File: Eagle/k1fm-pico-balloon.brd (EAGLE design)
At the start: 26.4 x 41.1 mm, 42 parts, among them J1 I2C, J2 ICSP, J3 SERIAL, J4 POWER, Q1 ASTX-H11-25.000MHZ-T, Q2 DMP2305U, Q3 DMP2305U, U1 ATMEGA328, U2 Si5351A-B-GT, U3 MCP1754X-XXXXX/C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

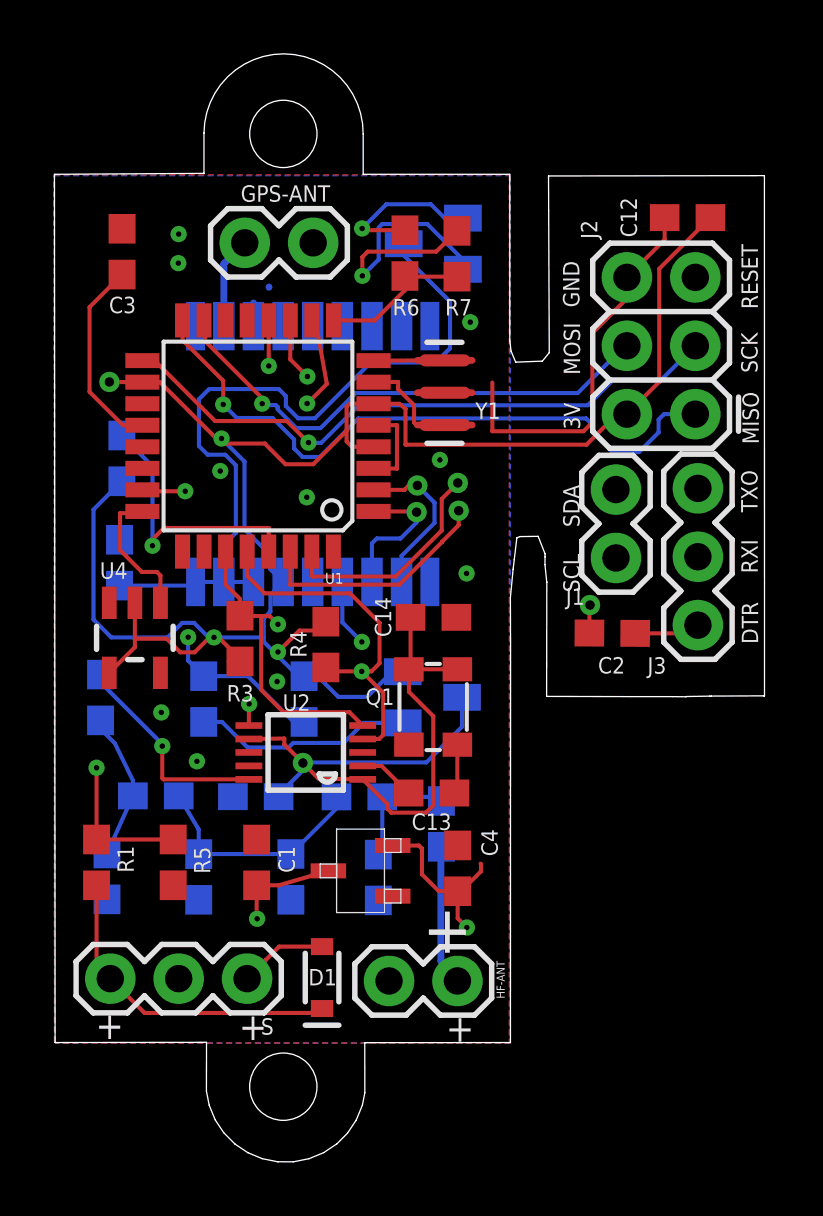
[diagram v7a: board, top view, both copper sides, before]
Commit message: Use PD2 (ext int) and PD5 (T1) for calibration
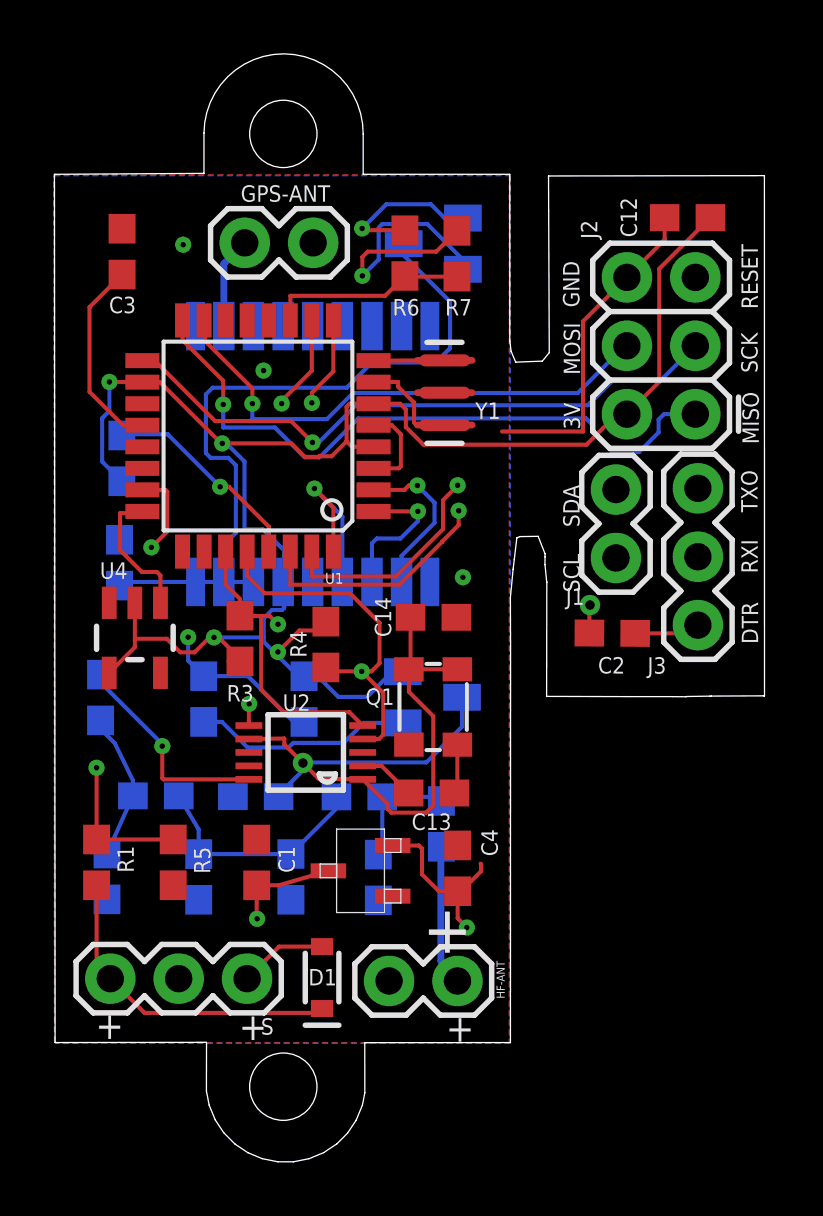
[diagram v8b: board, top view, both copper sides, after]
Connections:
- net CLK2: now also U1.9; no longer U1.11
- net GPS_E: now also U1.11; no longer U1.9
- net TIMEP: now also U1.32; no longer U1.12
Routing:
- net 3V: track 138.5 -> 110.6 mm
- net TIMEP: track 24.6 -> 6.53 mm, vias 2 -> 1
- net TX_E: track 28.6 -> 20.0 mm
- net RESET: track 55.1 -> 49.9 mm
- net GND: track 20.1 -> 15.6 mm, vias 10 -> 3
- net GPS_E: track 5.59 -> 7.42 mm
- net VDD_TST: track 19.2 -> 17.9 mm
- net N$8: track 28.8 -> 27.6 mm
